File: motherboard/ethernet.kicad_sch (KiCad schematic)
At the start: 13 parts, among them U15 LPJM4938GENL, U16 TPD4EUSB30, U17 TPD4EUSB30

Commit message: linked all footprints
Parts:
- R53, R54, R55, R56: footprint (none) -> Resistor_SMD:R_0402_1005Metric
- U15: footprint (none) -> Connector_RJ:RJ45_Wuerth_7499111446_Horizontal
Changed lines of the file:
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@@
 			)
 		)
-		(property "Footprint" ""
+		(property "Footprint" "Resistor_SMD:R_0402_1005Metric"
 			(at 146.05 66.04 0)
 			(effects
@@
 			)
 		)
-		(property "Footprint" ""
+		(property "Footprint" "Resistor_SMD:R_0402_1005Metric"
 			(at 148.59 66.04 0)
 			(effects
@@
 			)
 		)
-		(property "Footprint" ""
+		(property "Footprint" "Connector_RJ:RJ45_Wuerth_7499111446_Horizontal"
 			(at 127 81.28 0)
 			(effects
@@
 			)
 		)
-		(property "Footprint" ""
+		(property "Footprint" "Resistor_SMD:R_0402_1005Metric"
 			(at 154.94 74.93 0)
 			(effects
@@
 			)
 		)
-		(property "Footprint" ""
+		(property "Footprint" "Resistor_SMD:R_0402_1005Metric"
 			(at 154.94 80.01 0)
 			(effects

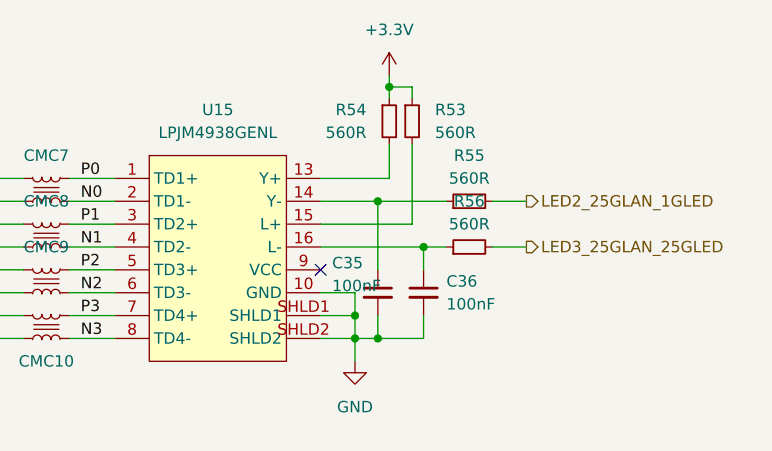
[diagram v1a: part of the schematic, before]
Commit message: cost optimizations for jlc
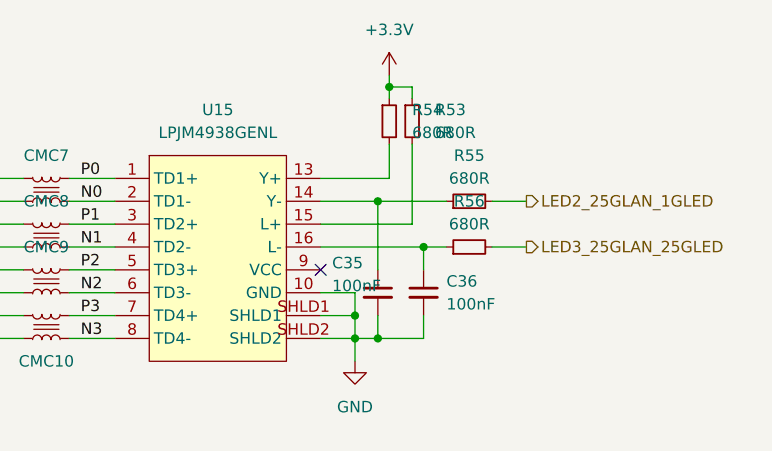
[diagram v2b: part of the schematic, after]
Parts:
- R53, R54, R55, R56: value 560R -> 680R
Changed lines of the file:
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@@
 		(fields_autoplaced yes)
 		(property "Reference" "R54"
-			(at 143.51 64.7699 0)
-			(effects
-				(font
-					(size 1.27 1.27)
-				)
-				(justify right)
-			)
-		)
-		(property "Value" "560R"
-			(at 143.51 67.3099 0)
-			(effects
-				(font
-					(size 1.27 1.27)
-				)
-				(justify right)
+			(at 148.59 64.7699 0)
+			(effects
+				(font
+					(size 1.27 1.27)
+				)
+				(justify left)
+			)
+		)
+		(property "Value" "680R"
+			(at 148.59 67.3099 0)
+			(effects
+				(font
+					(size 1.27 1.27)
+				)
+				(justify left)
 			)
 		)
@@
 			)
 		)
-		(property "Value" "560R"
+		(property "Value" "680R"
 			(at 151.13 67.3099 0)
 			(effects
@@
 			)
 		)
-		(property "Value" "560R"
+		(property "Value" "680R"
 			(at 154.94 72.39 90)
 			(effects
@@
 			)
 		)
-		(property "Value" "560R"
+		(property "Value" "680R"
 			(at 154.94 77.47 90)
 			(effects

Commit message: work preparing for routing
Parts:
- removed C35, C36: 100nF, Capacitor_SMD:C_0402_1005Metric, symbol Device:C_Small
- removed R55, R56: 680R, Resistor_SMD:R_0402_1005Metric, symbol Device:R_Small
- removed U15: LPJM4938GENL, Connector_RJ:RJ45_Wuerth_7499111446_Horizontal, symbol library:LPJM4938GENL
- added C94, C95, C96, C97: 100nF/100V, Capacitor_SMD:C_0402_1005Metric, symbol Device:C_Small
- added J23: L829-1J1T-JM, Ethernet:BEL_L829-1J1T-JM, symbol Ethernet:L829-1J1T-JM
- added TP1: RJ45 ORANGE LED, TestPoint:TestPoint_Pad_D2.0mm, symbol Connector:TestPoint_Alt
- R53, R54: value 680R -> 1k
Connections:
- net GND: now also C94.2, C95.2, C96.2, C97.2, J23.S1 (SHIELD), J23.S2 (SHIELD)
- net LED2_25GLAN_1GLED: now also J23.13
- net LED3_25GLAN_25GLED: now also J23.17
- net N0: now also J23.10 (TRD1-)
- net N1: now also J23.5 (TRD2-)
- net N2: now also J23.2 (TRD3-)
- net N3: now also J23.9 (TRD4-)
- net P0: now also J23.11 (TRD1+)
- net P1: now also J23.4 (TRD2+)
- net P2: now also J23.3 (TRD3+)
- net P3: now also J23.8 (TRD4+)
- net at R54.2: now also J23.16
- net at R53.2: now also J23.14
- new net: J23.15, TP1.1
- new net CT1: C94.1, J23.12 (TRCT1)
- new net CT2: C95.1, J23.6 (TRCT2)
- new net CT3: C96.1, J23.1 (TRCT3)
- new net CT4: C97.1, J23.7 (TRCT4)
- no-connect marks 1 -> 0

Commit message: component placement of I/O
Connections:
- net N0: now also CMC7.4; no longer CMC7.3
- net N1: now also CMC8.4; no longer CMC8.3
- net N2: now also CMC9.4; no longer CMC9.3
- net N3: now also CMC10.4; no longer CMC10.3
- net P0: now also CMC7.3; no longer CMC7.4
- net P1: now also CMC8.3; no longer CMC8.4
- net P2: now also CMC9.3; no longer CMC9.4
- net P25G_MDIN0: now also CMC7.1; no longer CMC7.2
- net P25G_MDIN1: now also CMC8.1; no longer CMC8.2
- net P25G_MDIN2: now also CMC9.1; no longer CMC9.2
- net P25G_MDIN3: now also CMC10.1; no longer CMC10.2
- net P25G_MDIP0: now also CMC7.2; no longer CMC7.1
- net P25G_MDIP1: now also CMC8.2; no longer CMC8.1
- net P25G_MDIP2: now also CMC9.2; no longer CMC9.1
- net P25G_MDIP3: now also CMC10.2; no longer CMC10.1
- net P3: now also CMC10.3; no longer CMC10.4

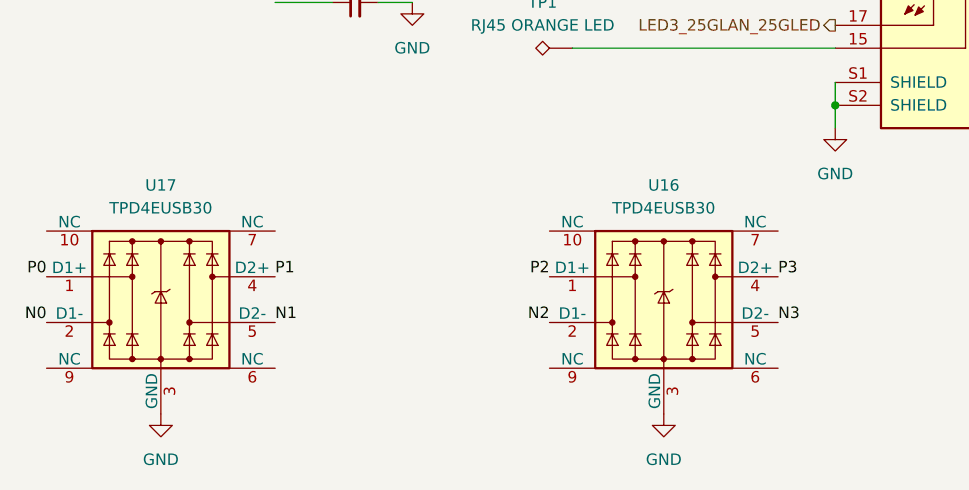
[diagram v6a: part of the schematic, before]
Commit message: placement roughly halfway done
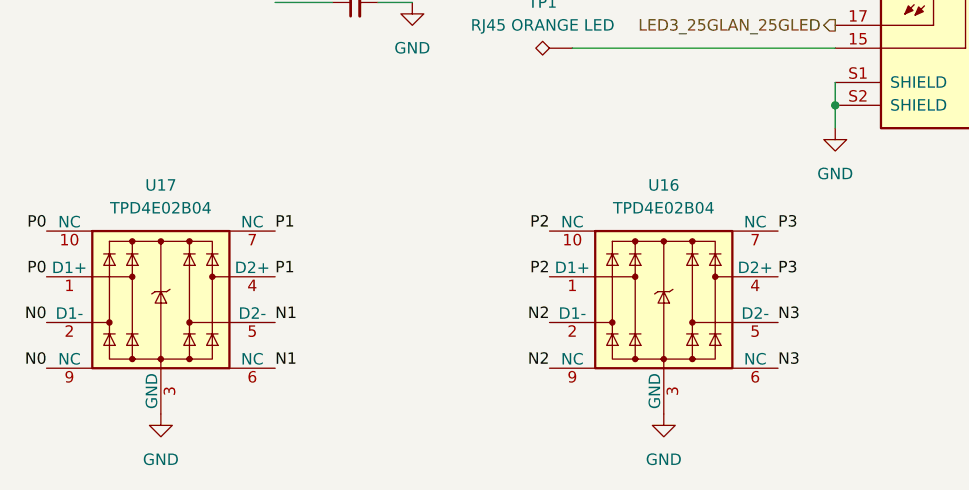
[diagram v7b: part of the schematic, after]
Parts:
- C94, C95, C96, C97: footprint Capacitor_SMD:C_0402_1005Metric -> Capacitor_SMD:C_0805_2012Metric
- U16, U17: value TPD4EUSB30 -> TPD4E02B04
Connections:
- net N0: now also U17.9 (NC)
- net N1: now also U17.6 (NC)
- net N2: now also U16.9 (NC)
- net N3: now also U16.6 (NC)
- net P0: now also U17.10 (NC)
- net P1: now also U17.7 (NC)
- net P2: now also U16.10 (NC)
- net P3: now also U16.7 (NC)
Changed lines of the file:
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@@
+		)
+	)
+	(label "P0"
+		(at 90.17 109.22 180)
+		(fields_autoplaced yes)
+		(effects
+			(font
+				(size 1.27 1.27)
+			)
+			(justify right bottom)
 		)
 	)
@@
 		)
 	)
+	(label "P3"
+		(at 171.45 109.22 0)
+		(fields_autoplaced yes)
+		(effects
+			(font
+				(size 1.27 1.27)
+			)
+			(justify left bottom)
+		)
+	)
+	(label "P1"
+		(at 115.57 109.22 0)
+		(fields_autoplaced yes)
+		(effects
+			(font
+				(size 1.27 1.27)
+			)
+			(justify left bottom)
+		)
+	)
 	(label "N0"
 		(at 165.1 35.56 0)
@@
 		)
 	)
+	(label "P2"
+		(at 146.05 109.22 180)
+		(fields_autoplaced yes)
+		(effects
+			(font
+				(size 1.27 1.27)
+			)
+			(justify right bottom)
+		)
+	)
 	(label "CT3"
 		(at 171.45 54.61 0)
@@
 		)
 	)
+	(label "N0"
+		(at 90.17 124.46 180)
+		(fields_autoplaced yes)
+		(effects
+			(font
+				(size 1.27 1.27)
+			)
+			(justify right bottom)
+		)
+	)
 	(label "N1"
 		(at 115.57 119.38 0)
@@
 	)
 	(label "N2"
+		(at 146.05 124.46 180)
+		(fields_autoplaced yes)
+		(effects
+			(font
+				(size 1.27 1.27)
+			)
+			(justify right bottom)
+		)
+	)
+	(label "N1"
+		(at 115.57 124.46 0)
+		(fields_autoplaced yes)
+		(effects
+			(font
+				(size 1.27 1.27)
+			)
+			(justify left bottom)
+		)
+	)
+	(label "N2"
 		(at 146.05 119.38 180)
 		(fields_autoplaced yes)
@@
 	(label "CT3"
 		(at 115.57 72.39 0)
+		(fields_autoplaced yes)
+		(effects
+			(font
+				(size 1.27 1.27)
+			)
+			(justify left bottom)
+		)
+	)
+	(label "N3"
+		(at 171.45 124.46 0)
 		(fields_autoplaced yes)
 		(effects
@@
 			)
 		)
-		(property "Footprint" "Capacitor_SMD:C_0402_1005Metric"
+		(property "Footprint" "Capacitor_SMD:C_0805_2012Metric"
 			(at 124.46 49.53 0)
 			(effects
@@
 			)
 		)
-		(property "Footprint" "Capacitor_SMD:C_0402_1005Metric"
+		(property "Footprint" "Capacitor_SMD:C_0805_2012Metric"
 			(at 124.46 72.39 0)
 			(effects
@@
 			)
 		)
-		(property "Footprint" "Capacitor_SMD:C_0402_1005Metric"
+		(property "Footprint" "Capacitor_SMD:C_0805_2012Metric"
 			(at 124.46 83.82 0)
 			(effects
@@
 			)
 		)
-		(property "Footprint" "Capacitor_SMD:C_0402_1005Metric"
+		(property "Footprint" "Capacitor_SMD:C_0805_2012Metric"
 			(at 124.46 60.96 0)
 			(effects
@@
 			)
 		)
-		(property "Value" "TPD4EUSB30"
+		(property "Value" "TPD4E02B04"
 			(at 102.87 106.68 0)
 			(effects
@@
 			)
 		)
-		(property "Value" "TPD4EUSB30"
+		(property "Value" "TPD4E02B04"
 			(at 158.75 106.68 0)
 			(effects
